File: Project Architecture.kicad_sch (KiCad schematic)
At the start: 0 parts

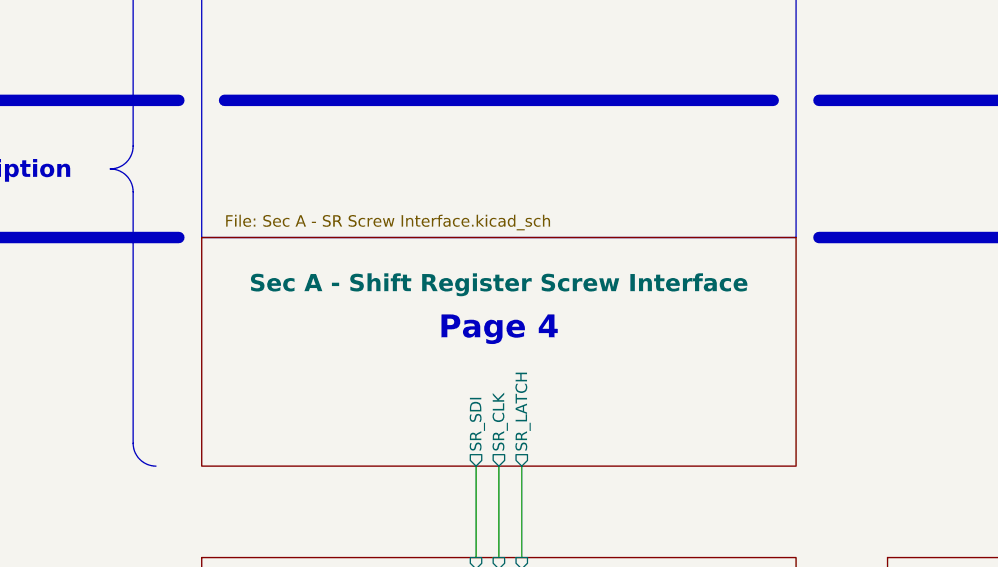
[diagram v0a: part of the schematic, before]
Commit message: documentation update / release 2.1.1 prep
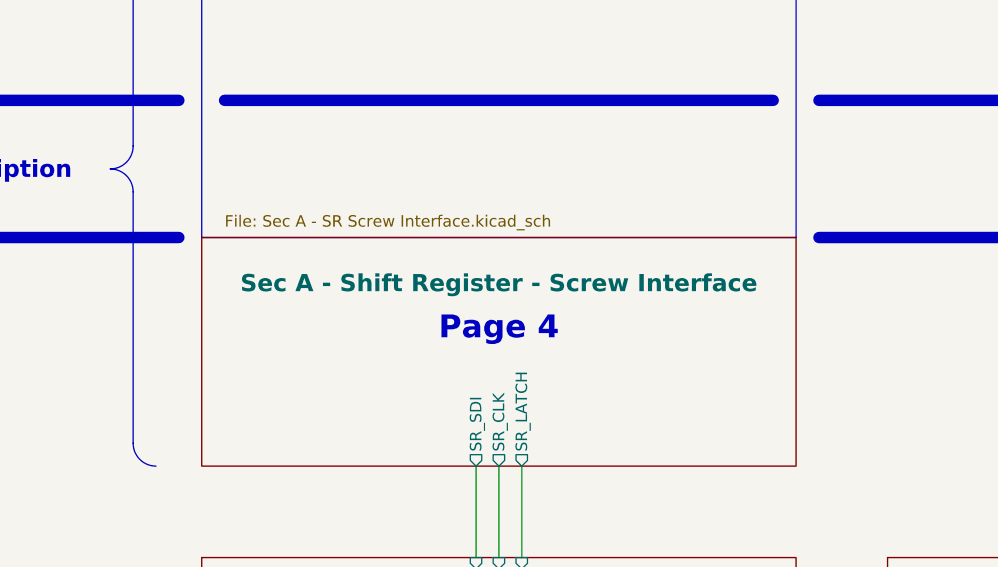
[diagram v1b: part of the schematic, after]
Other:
- sheet Sec A - Shift Register Screw Interface renamed Sec A - Shift Register - Screw Interface
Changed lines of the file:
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@@
 			(color 128 255 128 0.5000)
 		)
-		(property "Sheetname" "Sec A - Shift Register Screw Interface"
+		(property "Sheetname" "Sec A - Shift Register - Screw Interface"
 			(at 200.66 154.94 0)
 			(effects
